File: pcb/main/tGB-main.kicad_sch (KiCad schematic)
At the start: 70 parts, among them J1 GB-CardEdge, J2 PROG_PORT, Q1 DMG3415U, Q2 HN4A56JU, Q3 2N7002K, U1 TC74LCXR163245FT, U2 TC74LCXR163245FT, U3 ICE40UP5K-SG48ITR, U4 TPS79901DDCR, U5 TPS79901DDCR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

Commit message: common symbols and footprints
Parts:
- J2: footprint PinHeader:PinHeader-10P-Sidemount -> Pin_Sidemount:PinHeader_1x10_P2.54_Sidemount
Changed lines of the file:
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@@
     (property "Reference" "J2" (id 0) (at 295.91 49.53 0))
     (property "Value" "PROG_PORT" (id 1) (at 295.91 80.01 0))
-    (property "Footprint" "PinHeader:PinHeader-10P-Sidemount" (id 2) (at 295.91 63.5 0)
+    (property "Footprint" "Pin_Sidemount:PinHeader_1x10_P2.54_Sidemount" (id 2) (at 295.91 63.5 0)
       (effects (font (size 1.27 1.27)) hide)
     )
@@
     )
     (path "/00000000-0000-0000-0000-00006027ac0d"
-      (reference "J2") (unit 1) (value "PROG_PORT") (footprint "PinHeader:PinHeader-10P-Sidemount")
+      (reference "J2") (unit 1) (value "PROG_PORT") (footprint "Pin_Sidemount:PinHeader_1x10_P2.54_Sidemount")
     )
     (path "/d5f93cc2-b1a6-4187-bb4c-8f284d837e5c"

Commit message: set title and revision
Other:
- title: tsuraraGB main board -> tsuraraGB Main PCB
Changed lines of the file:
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@@
   (paper "A3")
   (title_block
-    (title "tsuraraGB main board")
+    (title "tsuraraGB Main PCB")
     (rev "B")
   )

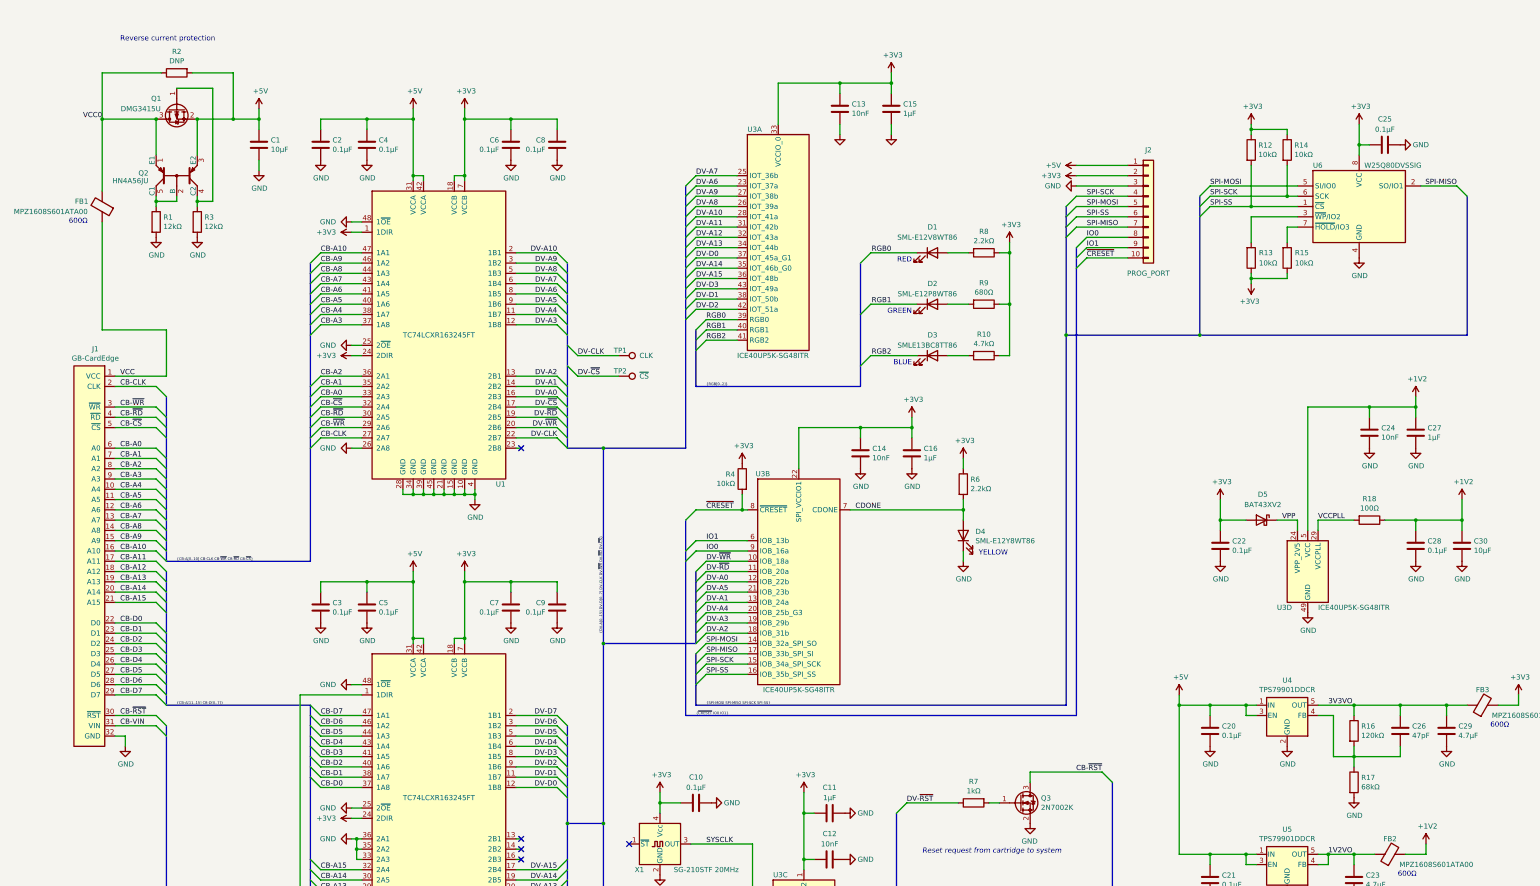
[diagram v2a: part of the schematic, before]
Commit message: migration from KiCad 6 to 7
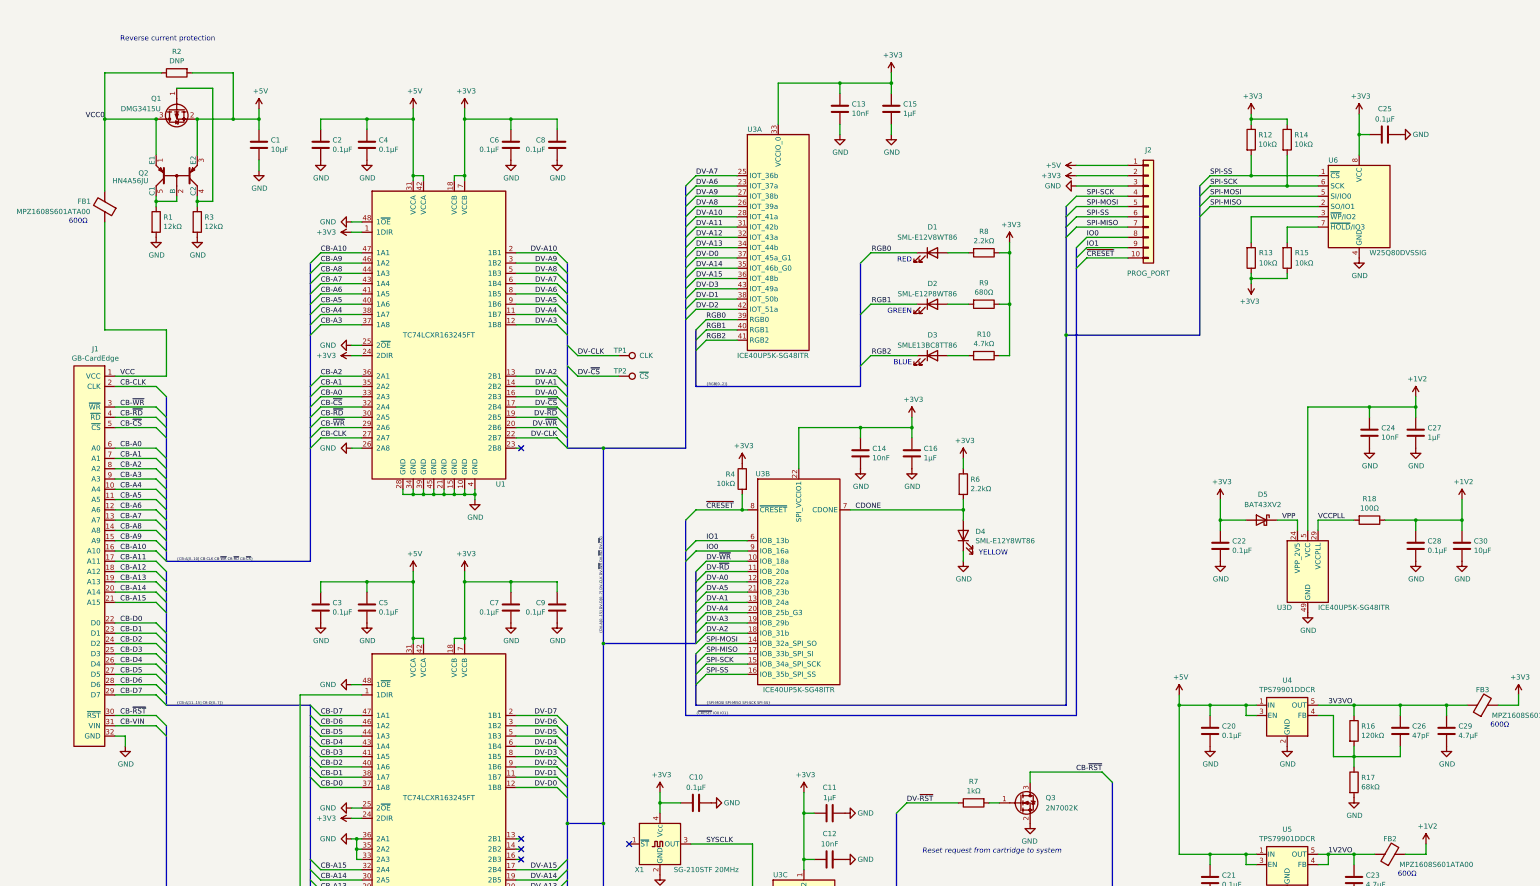
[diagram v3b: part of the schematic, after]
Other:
- moved on the sheet: C25, FB1, R12, R14, U6

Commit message: migrate KiCad 7 -> 10
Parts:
- C19: value 1uF -> 1μF
- D1, D2, D3, D4: footprint LED_SMD:LED_0603_1608Metric_Castellated -> ProjectSpecific:LED_0603_1608Metric_Castellated
- J1: footprint GB-CardEdge:GB-CardEdge -> ProjectSpecific:GB-CardEdge; symbol GB-CardEdge:GB-CardEdge -> ProjectSpecific:GB-CardEdge
- J2: footprint Pin_Sidemount:PinHeader_1x10_P2.54_Sidemount -> ProjectSpecific:PinHeader_1x10_P2.54_Sidemount
- Q1: symbol Device:Q_PMOS_GSD -> Transistor_FET:Q_PMOS_GSD
- Q2: symbol HN4A56JU:HN4A56JU -> ProjectSpecific:HN4A56JU
- U1, U2: symbol TC74LCXR163245FT:TC74LCXR163245FT -> ProjectSpecific:TC74LCXR163245FT
- U4, U5: symbol TPS79901DDCR:TPS79901DDCR -> ProjectSpecific:TPS79901DDCR
- U6: footprint Package_SO:SOIC-8_5.275x5.275mm_P1.27mm -> Package_SO:SOIC-8_5.3x5.3mm_P1.27mm
